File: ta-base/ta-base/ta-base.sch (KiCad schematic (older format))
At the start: 3 parts

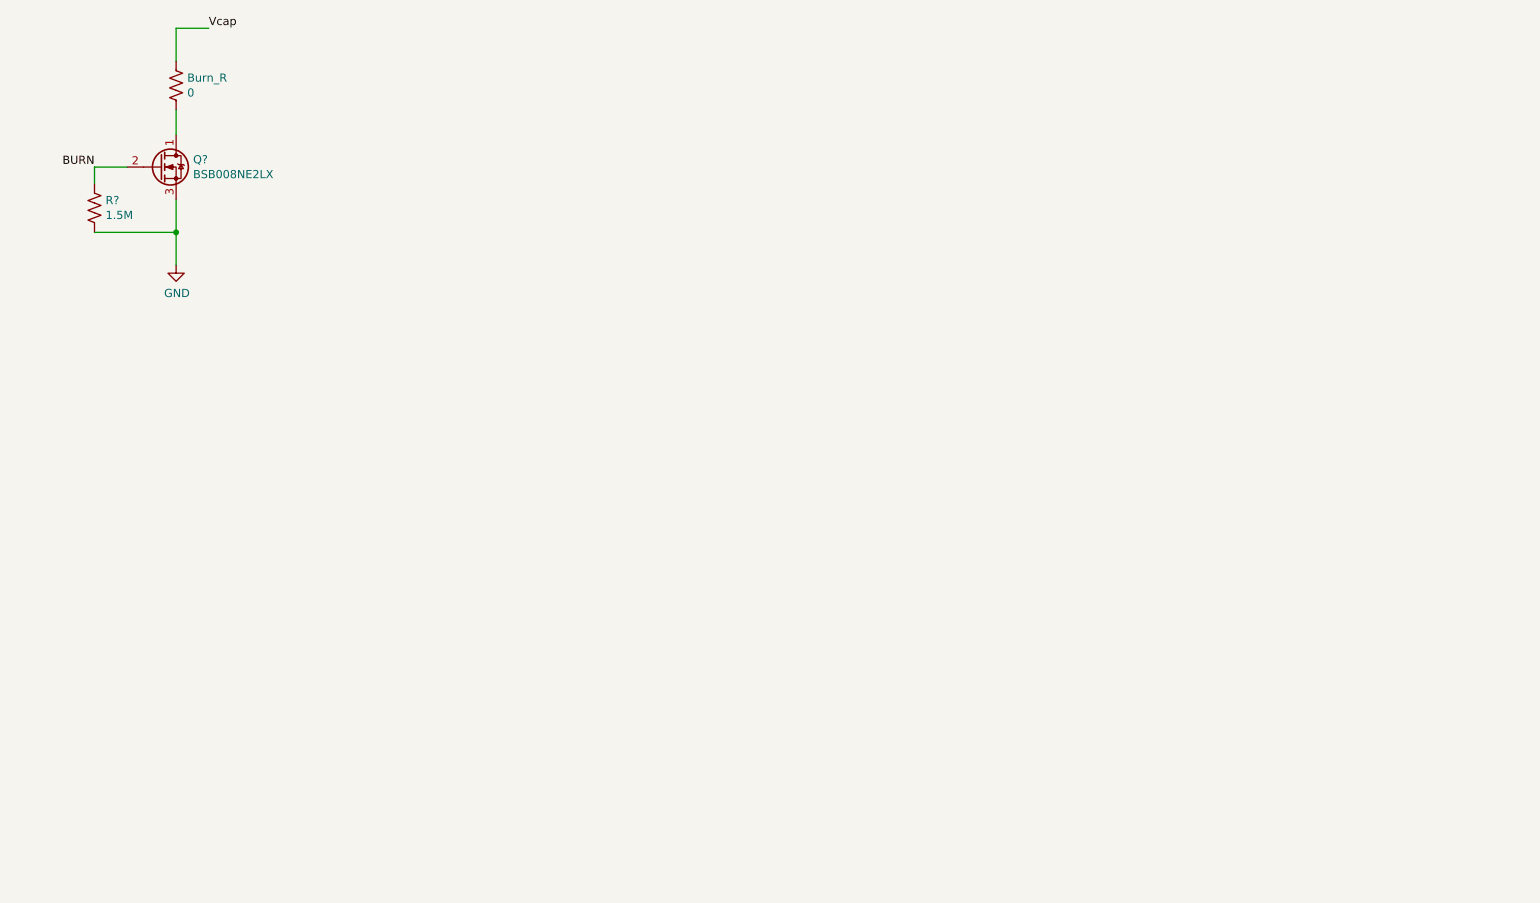
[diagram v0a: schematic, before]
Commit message: Need to patch symbols and footprints together and route
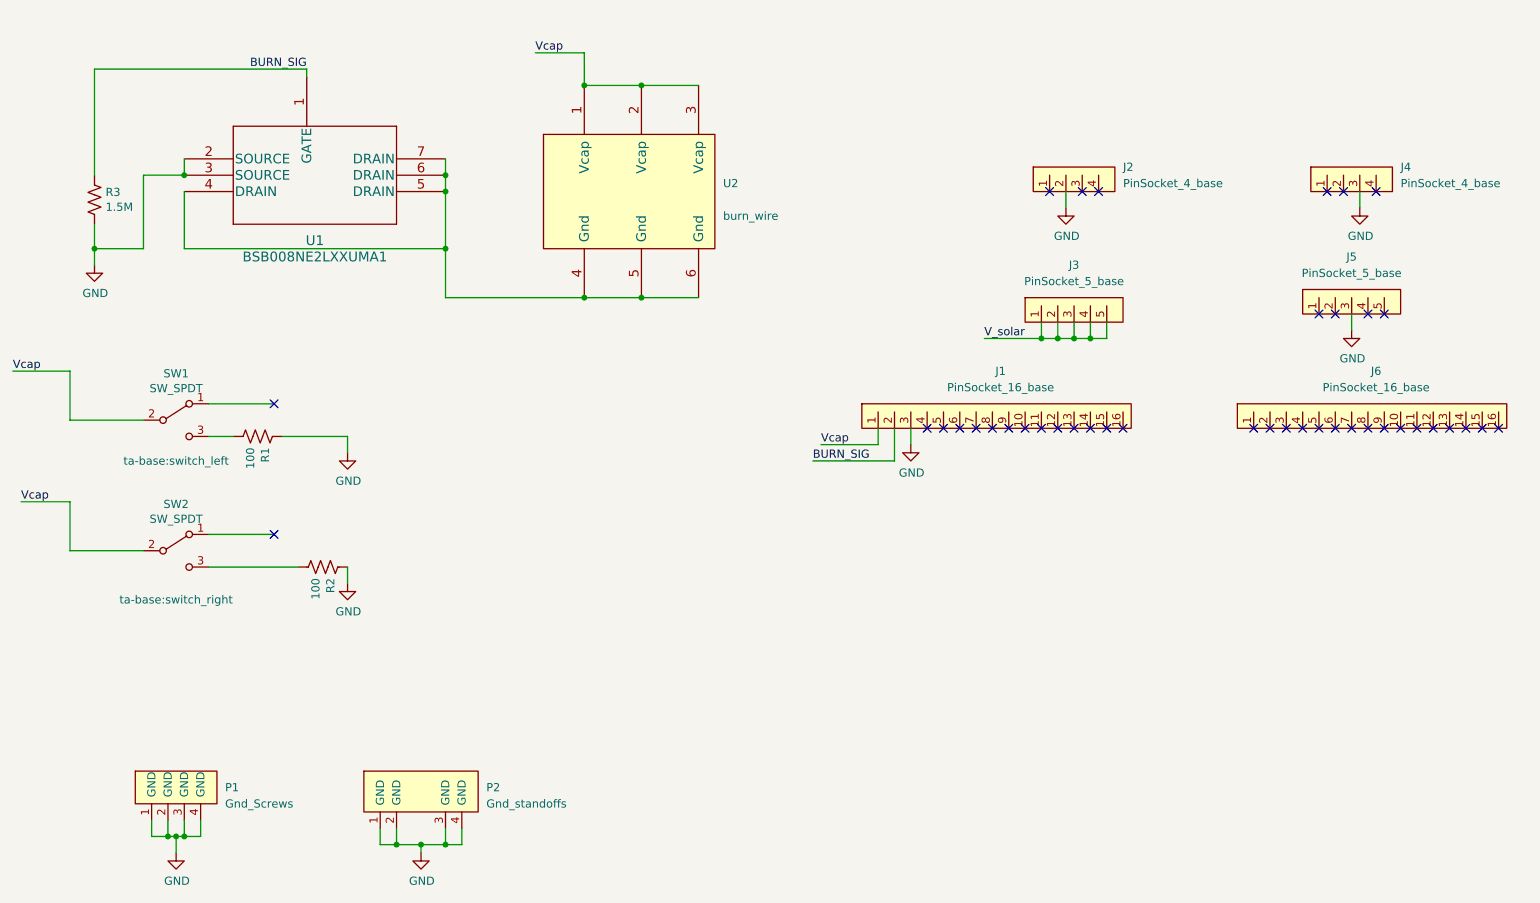
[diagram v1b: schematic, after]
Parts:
- removed Burn_R: 0, symbol Device:R_US
- removed Q?: BSB008NE2LX, Package_DirectFET:DirectFET_MX, symbol Transistor_FET:BSB008NE2LX
- added J1: PinSocket_16_base, ta-base:PinSocket_1x16_TartanArtibeus_base_cpy, symbol ta-base:PinSocket_16_base
- added J2: PinSocket_4_base, ta-base:PinSocket_1x4_TartanArtibeus_base_cpy, symbol ta-base:PinSocket_4_base
- added J3, J5: PinSocket_5_base, symbol ta-base:PinSocket_5_base
- added J4: PinSocket_4_base, symbol ta-base:PinSocket_4_base
- added J6: PinSocket_16_base, symbol ta-base:PinSocket_16_base
- added P1: Gnd_Screws, ta-base:chassis_gnd_screws, symbol ta-base:Gnd_Screws
- added P2: Gnd_standoffs, ta-base:MountingHoles_TartanArtibeus_base_cpy, symbol ta-base:Gnd_standoffs
- added R1, R2: 100, ta-base:R_0603_1608Metric_base_cpy, symbol Device:R_US
- added SW1: SW_SPDT, ta-base:switch_left, symbol Switch:SW_SPDT
- added SW2: SW_SPDT, ta-base:switch_right, symbol Switch:SW_SPDT
- added U1: BSB008NE2LXXUMA1, ta-base:BSB008NE2LXXUMA1, symbol infineon:BSB008NE2LXXUMA1
- added U2: burn_wire, ta-base:burn_wire, symbol ta-base:burn_wire
- R3: renamed from R?; footprint (none) -> ta-base:R_0603_1608Metric_base_cpy; Manufacturer (none) -> Vishay; Part number (none) -> CRCW06031M50FKEB; Supplier (none) -> Mouser; Supplier Part number (none) -> 71-CRCW06031M50FKEB
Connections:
- net GND: now also J1.3, J2.2, J4.3, J5.3, P1.1 (GND), P1.2 (GND), P1.3 (GND), P1.4 (GND), P2.1 (GND), P2.2 (GND), P2.3 (GND), P2.4 (GND), R1.1, R2.1, U1.2 (SOURCE), U1.3 (SOURCE)
- net Vcap: now also J1.1, SW1.2 (B), SW2.2 (B), U2.1 (Vcap), U2.2 (Vcap), U2.3 (Vcap)
- net BURN renamed BURN_SIG
- net BURN_SIG: now also J1.2, U1.1 (GATE)
- new net: R1.2, SW1.3 (C)
- new net: R2.2, SW2.3 (C)
- new net: U1.4 (DRAIN), U1.5 (DRAIN), U1.6 (DRAIN), U1.7 (DRAIN), U2.4 (Gnd), U2.5 (Gnd), U2.6 (Gnd)
- new net V_solar: J3.1, J3.2, J3.3, J3.4, J3.5
- no-connect marks 0 -> 41
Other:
- moved on the sheet: R3

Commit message: finalized place and route
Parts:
- removed J3: PinSocket_5_base, symbol ta-base:PinSocket_5_base
- added J3: PinSocket_4_base, ta-base:PinSocket_1x4_TartanArtibeus_base_cpy, symbol ta-base:PinSocket_4_base
- added J7, J8: PinSocket_5_base, ta-base:solar_internal, symbol ta-base:PinSocket_5_base
- J4: footprint (none) -> ta-base:PinSocket_1x4_TartanArtibeus_base_cpy
- J5: footprint (none) -> ta-base:PinSocket_1x5_right_TartanArtibeus_base_cpy
- J6: footprint (none) -> ta-base:PinSocket_1x16_TartanArtibeus_base_cpy
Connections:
- net V_solar: now also J3.1, J3.2, J3.3, J3.4, J7.1, J7.2, J7.3, J7.4, J7.5, J8.1, J8.2, J8.3, J8.4, J8.5
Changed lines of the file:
@@
 F 0 "J4" H 10000 2100 50  0000 L CNN
 F 1 "PinSocket_4_base" H 10000 2000 50  0000 L CNN
-F 2 "" H 9650 1950 50  0001 C CNN
+F 2 "ta-base:PinSocket_1x4_TartanArtibeus_base_cpy" H 9650 1950 50  0001 C CNN
 F 3 "" H 9650 1950 50  0001 C CNN
 	1    9700 1950
-	1    0    0    -1
-$EndComp
-$Comp
-L ta-base:PinSocket_5_base J3
-U 1 1 60FD2C19
-P 8000 2750
-F 0 "J3" H 8000 3100 50  0000 C CNN
-F 1 "PinSocket_5_base" H 8000 3000 50  0000 C CNN
-F 2 "" H 7900 2750 50  0001 C CNN
-F 3 "" H 7900 2750 50  0001 C CNN
-	1    8000 2750
 	1    0    0    -1
 $EndComp
@@
 F 0 "J5" H 9700 3050 50  0000 C CNN
 F 1 "PinSocket_5_base" H 9700 2950 50  0000 C CNN
-F 2 "" H 9600 2700 50  0001 C CNN
+F 2 "ta-base:PinSocket_1x5_right_TartanArtibeus_base_cpy" H 9600 2700 50  0001 C CNN
 F 3 "" H 9600 2700 50  0001 C CNN
 	1    9700 2700
@@
 F 0 "J6" H 9850 3750 50  0000 C CNN
 F 1 "PinSocket_16_base" H 9850 3650 50  0000 C CNN
-F 2 "" H 9400 3400 50  0001 C CNN
+F 2 "ta-base:PinSocket_1x16_TartanArtibeus_base_cpy" H 9400 3400 50  0001 C CNN
 F 3 "" H 9400 3400 50  0001 C CNN
 	1    9800 3400
@@
 $EndComp
 Wire Wire Line
-	7800 2750 7800 2850
-Wire Wire Line
-	7800 2850 7900 2850
-Wire Wire Line
-	8200 2850 8200 2750
-Wire Wire Line
-	8100 2750 8100 2850
-Connection ~ 8100 2850
-Wire Wire Line
-	8100 2850 8200 2850
-Wire Wire Line
-	8000 2750 8000 2850
-Connection ~ 8000 2850
-Wire Wire Line
-	8000 2850 8100 2850
-Wire Wire Line
-	7900 2750 7900 2850
-Connection ~ 7900 2850
-Wire Wire Line
-	7900 2850 8000 2850
-Wire Wire Line
-	7800 2850 7450 2850
-Connection ~ 7800 2850
-Text Label 7450 2850 0    50   ~ 0
+	7850 2700 7850 2800
+Wire Wire Line
+	7850 2800 7950 2800
+Wire Wire Line
+	8150 2700 8150 2800
+Wire Wire Line
+	8050 2700 8050 2800
+Connection ~ 8050 2800
+Wire Wire Line
+	8050 2800 8150 2800
+Wire Wire Line
+	7950 2700 7950 2800
+Connection ~ 7950 2800
+Wire Wire Line
+	7950 2800 8050 2800
+Wire Wire Line
+	7850 2800 7500 2800
+Connection ~ 7850 2800
+Text Label 7500 2800 0    50   ~ 0
 V_solar
 Wire Wire Line
@@
 Wire Wire Line
 	4000 5950 4150 5950
+$Comp
+L ta-base:PinSocket_4_base J3
+U 1 1 60FB8139
+P 8000 2700
+F 0 "J3" H 8300 2850 50  0000 L CNN
+F 1 "PinSocket_4_base" H 8300 2750 50  0000 L CNN
+F 2 "ta-base:PinSocket_1x4_TartanArtibeus_base_cpy" H 7950 2700 50  0001 C CNN
+F 3 "" H 7950 2700 50  0001 C CNN
+	1    8000 2700
+	1    0    0    -1
+$EndComp
+Wire Wire Line
+	8700 4500 9050 4500
+Connection ~ 9050 4500
+Wire Wire Line
+	9050 4400 9050 4500
+Text Label 8700 4500 0    50   ~ 0
+V_solar
+Connection ~ 9250 4500
+Wire Wire Line
+	9250 4400 9250 4500
+Wire Wire Line
+	9250 4500 9350 4500
+Wire Wire Line
+	9350 4500 9450 4500
+Connection ~ 9350 4500
+Wire Wire Line
+	9350 4400 9350 4500
+Wire Wire Line
+	9450 4400 9450 4500
+Wire Wire Line
+	9150 4500 9050 4500
+Wire Wire Line
+	9150 4500 9250 4500
+Connection ~ 9150 4500
+Wire Wire Line
+	9150 4400 9150 4500
+$Comp
+L ta-base:PinSocket_5_base J8
+U 1 1 60FF8354
+P 9250 4400
+F 0 "J8" H 9250 4750 50  0000 C CNN
+F 1 "PinSocket_5_base" H 9250 4650 50  0000 C CNN
+F 2 "ta-base:solar_internal" H 9150 4400 50  0001 C CNN
+F 3 "" H 9150 4400 50  0001 C CNN
+	1    9250 4400
+	1    0    0    -1
+$EndComp
+Wire Wire Line
+	7450 4500 7800 4500
+Connection ~ 7800 4500
+Wire Wire Line
+	7800 4400 7800 4500
+Text Label 7450 4500 0    50   ~ 0
+V_solar
+Connection ~ 8000 4500
+Wire Wire Line
+	8000 4400 8000 4500
+Wire Wire Line
+	8000 4500 8100 4500
+Wire Wire Line
+	8100 4500 8200 4500
+Connection ~ 8100 4500
+Wire Wire Line
+	8100 4400 8100 4500
+Wire Wire Line
+	8200 4400 8200 4500
+Wire Wire Line
+	7900 4500 7800 4500
+Wire Wire Line
+	7900 4500 8000 4500
+Connection ~ 7900 4500
+Wire Wire Line
+	7900 4400 7900 4500
+$Comp
+L ta-base:PinSocket_5_base J7
+U 1 1 60FE4BFB
+P 8000 4400
+F 0 "J7" H 8000 4750 50  0000 C CNN
+F 1 "PinSocket_5_base" H 8000 4650 50  0000 C CNN
+F 2 "ta-base:solar_internal" H 7900 4400 50  0001 C CNN
+F 3 "" H 7900 4400 50  0001 C CNN
+	1    8000 4400
+	1    0    0    -1
+$EndComp
 $EndSCHEMATC

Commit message: added new solar header
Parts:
- J7: footprint ta-base:solar_internal -> ta-base:5023860570
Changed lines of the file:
@@
 F 0 "J7" H 8000 4750 50  0000 C CNN
 F 1 "PinSocket_5_base" H 8000 4650 50  0000 C CNN
-F 2 "ta-base:solar_internal" H 7900 4400 50  0001 C CNN
+F 2 "ta-base:5023860570" H 7900 4400 50  0001 C CNN
 F 3 "" H 7900 4400 50  0001 C CNN
 	1    8000 4400

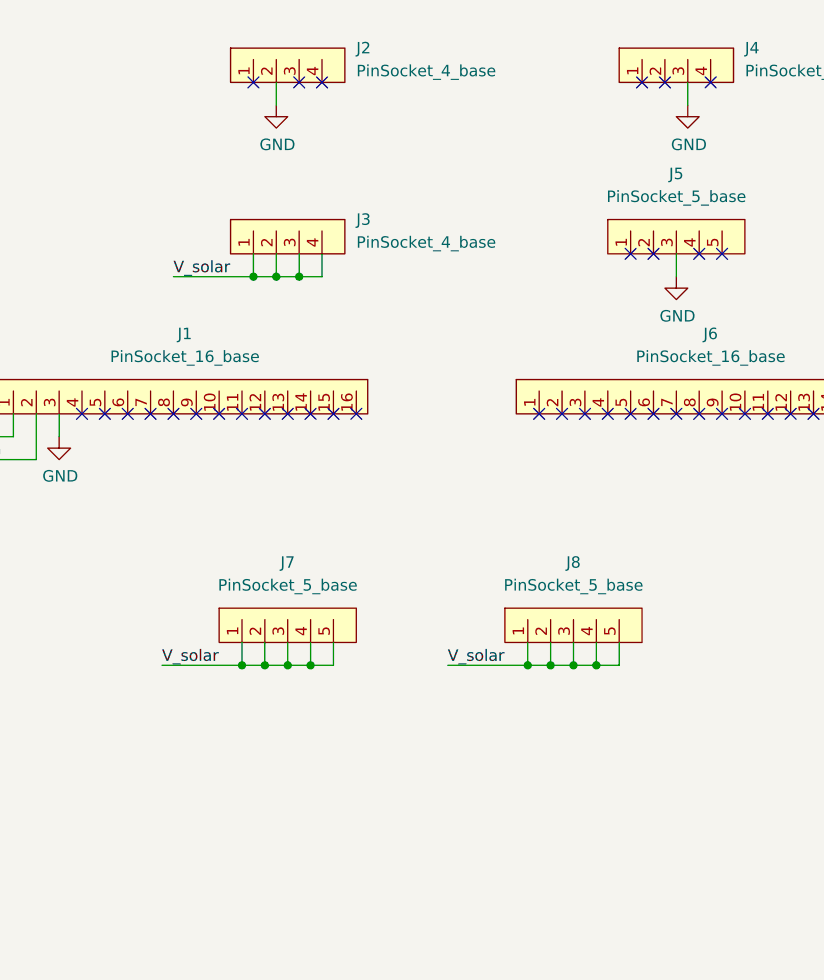
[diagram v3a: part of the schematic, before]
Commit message: added connector on outside
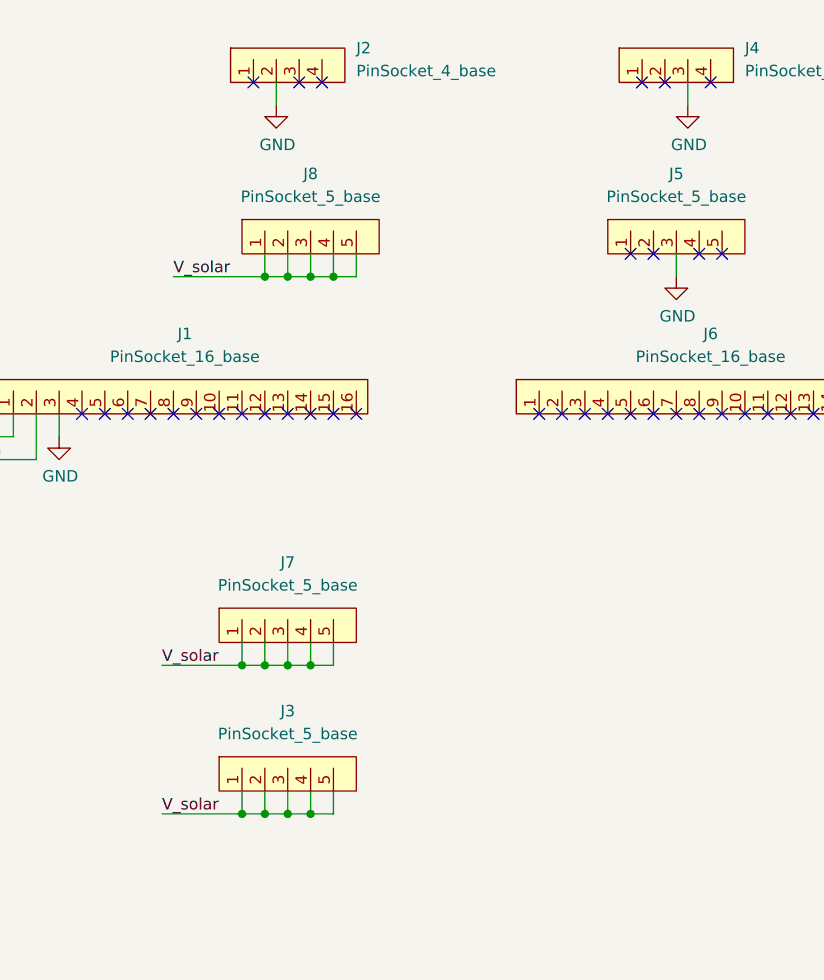
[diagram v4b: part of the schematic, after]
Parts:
- removed J3: PinSocket_4_base, ta-base:PinSocket_1x4_TartanArtibeus_base_cpy, symbol ta-base:PinSocket_4_base
- added J3: PinSocket_5_base, ta-base:5023860570, symbol ta-base:PinSocket_5_base
- J8: footprint ta-base:solar_internal -> ta-base:PinSocket_1x5_left_TartanArtibeus_base_cpy
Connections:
- net V_solar: now also J3.1, J3.2, J3.3, J3.4, J3.5
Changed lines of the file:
@@
 	1    0    0    -1
 $EndComp
-Wire Wire Line
-	7850 2700 7850 2800
-Wire Wire Line
-	7850 2800 7950 2800
-Wire Wire Line
-	8150 2700 8150 2800
-Wire Wire Line
-	8050 2700 8050 2800
-Connection ~ 8050 2800
-Wire Wire Line
-	8050 2800 8150 2800
-Wire Wire Line
-	7950 2700 7950 2800
-Connection ~ 7950 2800
-Wire Wire Line
-	7950 2800 8050 2800
-Wire Wire Line
-	7850 2800 7500 2800
-Connection ~ 7850 2800
 Text Label 7500 2800 0    50   ~ 0
 V_solar
@@
 Wire Wire Line
 	4000 5950 4150 5950
-$Comp
-L ta-base:PinSocket_4_base J3
-U 1 1 60FB8139
-P 8000 2700
-F 0 "J3" H 8300 2850 50  0000 L CNN
-F 1 "PinSocket_4_base" H 8300 2750 50  0000 L CNN
-F 2 "ta-base:PinSocket_1x4_TartanArtibeus_base_cpy" H 7950 2700 50  0001 C CNN
-F 3 "" H 7950 2700 50  0001 C CNN
-	1    8000 2700
-	1    0    0    -1
-$EndComp
-Wire Wire Line
-	8700 4500 9050 4500
-Connection ~ 9050 4500
-Wire Wire Line
-	9050 4400 9050 4500
-Text Label 8700 4500 0    50   ~ 0
-V_solar
-Connection ~ 9250 4500
-Wire Wire Line
-	9250 4400 9250 4500
-Wire Wire Line
-	9250 4500 9350 4500
-Wire Wire Line
-	9350 4500 9450 4500
-Connection ~ 9350 4500
-Wire Wire Line
-	9350 4400 9350 4500
-Wire Wire Line
-	9450 4400 9450 4500
-Wire Wire Line
-	9150 4500 9050 4500
-Wire Wire Line
-	9150 4500 9250 4500
-Connection ~ 9150 4500
-Wire Wire Line
-	9150 4400 9150 4500
-$Comp
-L ta-base:PinSocket_5_base J8
-U 1 1 60FF8354
-P 9250 4400
-F 0 "J8" H 9250 4750 50  0000 C CNN
-F 1 "PinSocket_5_base" H 9250 4650 50  0000 C CNN
-F 2 "ta-base:solar_internal" H 9150 4400 50  0001 C CNN
-F 3 "" H 9150 4400 50  0001 C CNN
-	1    9250 4400
-	1    0    0    -1
-$EndComp
 Wire Wire Line
 	7450 4500 7800 4500
@@
 	1    0    0    -1
 $EndComp
+$Comp
+L ta-base:PinSocket_5_base J8
+U 1 1 610118E5
+P 8100 2700
+F 0 "J8" H 8100 3050 50  0000 C CNN
+F 1 "PinSocket_5_base" H 8100 2950 50  0000 C CNN
+F 2 "ta-base:PinSocket_1x5_left_TartanArtibeus_base_cpy" H 8000 2700 50  0001 C CNN
+F 3 "" H 8000 2700 50  0001 C CNN
+	1    8100 2700
+	1    0    0    -1
+$EndComp
+Wire Wire Line
+	8300 2800 8300 2700
+Wire Wire Line
+	7500 2800 7900 2800
+Connection ~ 8200 2800
+Wire Wire Line
+	8200 2800 8300 2800
+Wire Wire Line
+	8200 2700 8200 2800
+Wire Wire Line
+	8100 2700 8100 2800
+Connection ~ 8100 2800
+Wire Wire Line
+	8100 2800 8200 2800
+Wire Wire Line
+	8000 2700 8000 2800
+Connection ~ 8000 2800
+Wire Wire Line
+	8000 2800 8100 2800
+Wire Wire Line
+	7900 2700 7900 2800
+Connection ~ 7900 2800
+Wire Wire Line
+	7900 2800 8000 2800
+Wire Wire Line
+	7450 5150 7800 5150
+Connection ~ 7800 5150
+Wire Wire Line
+	7800 5050 7800 5150
+Text Label 7450 5150 0    50   ~ 0
+V_solar
+Connection ~ 8000 5150
+Wire Wire Line
+	8000 5050 8000 5150
+Wire Wire Line
+	8000 5150 8100 5150
+Wire Wire Line
+	8100 5150 8200 5150
+Connection ~ 8100 5150
+Wire Wire Line
+	8100 5050 8100 5150
+Wire Wire Line
+	8200 5050 8200 5150
+Wire Wire Line
+	7900 5150 7800 5150
+Wire Wire Line
+	7900 5150 8000 5150
+Connection ~ 7900 5150
+Wire Wire Line
+	7900 5050 7900 5150
+$Comp
+L ta-base:PinSocket_5_base J3
+U 1 1 61022732
+P 8000 5050
+F 0 "J3" H 8000 5400 50  0000 C CNN
+F 1 "PinSocket_5_base" H 8000 5300 50  0000 C CNN
+F 2 "ta-base:5023860570" H 7900 5050 50  0001 C CNN
+F 3 "" H 7900 5050 50  0001 C CNN
+	1    8000 5050
+	1    0    0    -1
+$EndComp
